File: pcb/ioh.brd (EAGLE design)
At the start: 100 x 80 mm, 23 parts, among them Q1 MOSFET-NCHANNEL2N7000, Q2 MOSFET-NCHANNEL2N7000, Q3 MOSFET-NCHANNEL2N7000, Q4 MOSFET-NCHANNEL2N7000

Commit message: some names
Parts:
- renumbered D1 to IRFRONT, D2 to IRBACK, JP3 to BZZ
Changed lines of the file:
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@@
 <element name="Q1" library="SparkFun-DiscreteSemi" package="TO-92" value="MOSFET-NCHANNEL2N7000" x="-52.07" y="71.12"/>
 <element name="R1" library="SparkFun-Resistors" package="AXIAL-0.4" value="20k" x="-62.23" y="69.85"/>
-<element name="D1" library="SparkFun-LED" package="LTE-302" value="" x="-66.04" y="-1.27"/>
+<element name="IRFRONT" library="SparkFun-LED" package="LTE-302" value="" x="-66.04" y="-1.27"/>
 <element name="R2" library="SparkFun-Resistors" package="AXIAL-0.4" value="20k" x="-62.23" y="-6.35"/>
 <element name="Q2" library="SparkFun-DiscreteSemi" package="TO-92" value="MOSFET-NCHANNEL2N7000" x="-64.77" y="-11.43"/>
-<element name="D2" library="SparkFun-LED" package="LTE-302" value="" x="-66.04" y="-24.13"/>
+<element name="IRBACK" library="SparkFun-LED" package="LTE-302" value="" x="-66.04" y="-24.13"/>
 <element name="R3" library="SparkFun-Resistors" package="AXIAL-0.4" value="20k" x="-62.23" y="-21.59"/>
 <element name="Q3" library="SparkFun-DiscreteSemi" package="TO-92" value="MOSFET-NCHANNEL2N7000" x="-64.77" y="-16.51"/>
@@
 <attribute name="PROD_ID" value="CAP-08440" x="-72.39" y="-30.48" size="1.778" layer="27" display="off"/>
 </element>
-<element name="JP3" library="SparkFun-Connectors" package="1X02" value="M02PTH" x="-72.39" y="-39.37"/>
+<element name="BZZ" library="SparkFun-Connectors" package="1X02" value="M02PTH" x="-72.39" y="-39.37"/>
 <element name="Q4" library="SparkFun-DiscreteSemi" package="TO-92" value="MOSFET-NCHANNEL2N7000" x="-71.12" y="-46.99"/>
 <element name="S1" library="adafruit" package="B3F-40XX" value="" x="-66.04" y="-58.42">
@@
 <contactref element="R2" pad="P$2"/>
 <contactref element="R3" pad="P$2"/>
-<contactref element="JP3" pad="1"/>
+<contactref element="BZZ" pad="1"/>
 <wire x1="-57.15" y1="-21.59" x2="-72.39" y2="-39.37" width="0" layer="19" extent="1-1"/>
 <wire x1="-57.15" y1="-6.35" x2="-57.15" y2="-21.59" width="0" layer="19" extent="1-1"/>
@@
 <signal name="N$4">
 <contactref element="R2" pad="P$1"/>
-<contactref element="D1" pad="A"/>
+<contactref element="IRFRONT" pad="A"/>
 <wire x1="-64.77" y1="-1.27" x2="-67.31" y2="-6.35" width="0" layer="19" extent="1-1"/>
 </signal>
 <signal name="N$11">
-<contactref element="D1" pad="C"/>
+<contactref element="IRFRONT" pad="C"/>
 <contactref element="Q2" pad="3"/>
 <wire x1="-67.31" y1="-1.27" x2="-63.5" y2="-11.43" width="0" layer="19" extent="1-1"/>
@@
 <signal name="N$24">
 <contactref element="R3" pad="P$1"/>
-<contactref element="D2" pad="A"/>
+<contactref element="IRBACK" pad="A"/>
 <wire x1="-64.77" y1="-24.13" x2="-67.31" y2="-21.59" width="0" layer="19" extent="1-1"/>
 </signal>
 <signal name="N$25">
-<contactref element="D2" pad="C"/>
+<contactref element="IRBACK" pad="C"/>
 <contactref element="Q3" pad="3"/>
 <wire x1="-63.5" y1="-16.51" x2="-67.31" y2="-24.13" width="0" layer="19" extent="1-1"/>
@@
 <signal name="N$13">
 <contactref element="Q4" pad="3"/>
-<contactref element="JP3" pad="2"/>
+<contactref element="BZZ" pad="2"/>
 <wire x1="-69.85" y1="-39.37" x2="-69.85" y2="-46.99" width="0" layer="19" extent="1-1"/>
 </signal>

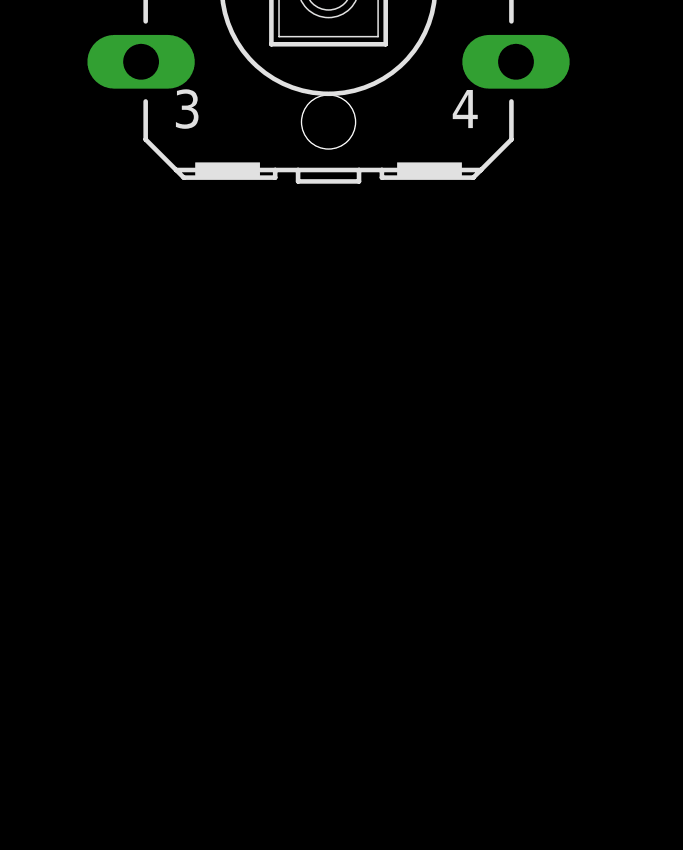
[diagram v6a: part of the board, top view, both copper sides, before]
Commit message: power test points
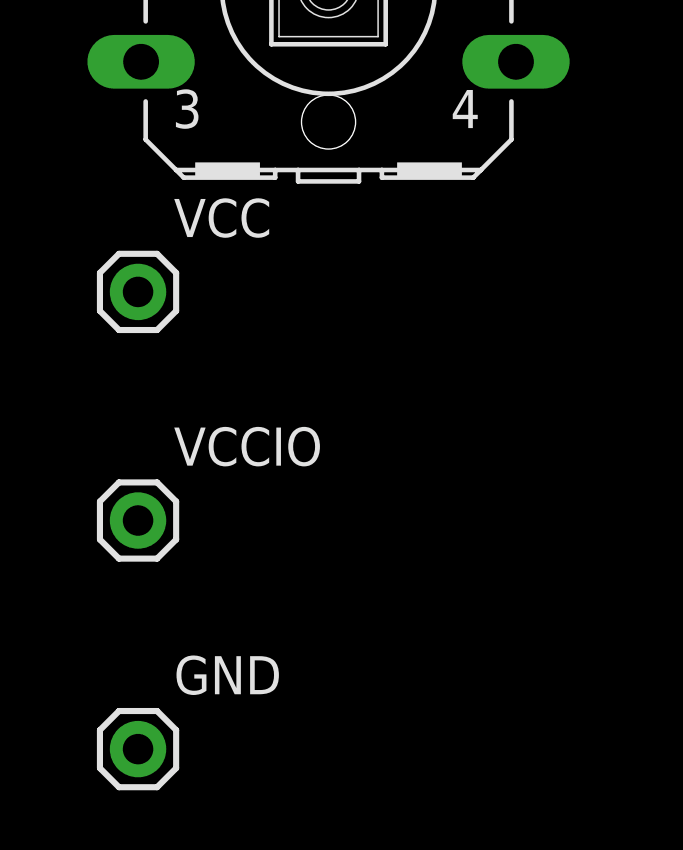
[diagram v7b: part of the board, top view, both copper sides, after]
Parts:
- added GND, VCC, VCCIO: M01PTH, SparkFun-Connectors:1X01
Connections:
- net GND: now also GND.1
- net VCC: now also VCC.1
- net VCCIO: now also VCCIO.1
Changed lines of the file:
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@@
 <attribute name="OC_FARNELL" value="176434" x="-66.04" y="-58.42" size="1.778" layer="27" display="off"/>
 </element>
+<element name="VCC" library="SparkFun-Connectors" package="1X01" value="M01PTH" x="-72.39" y="-68.58"/>
+<element name="VCCIO" library="SparkFun-Connectors" package="1X01" value="M01PTH" x="-72.39" y="-76.2"/>
+<element name="GND" library="SparkFun-Connectors" package="1X01" value="M01PTH" x="-72.39" y="-83.82"/>
 </elements>
 <signals>
@@
 <contactref element="S1" pad="3"/>
 <contactref element="S1" pad="4"/>
+<contactref element="GND" pad="1"/>
+<wire x1="-72.2884" y1="-60.9092" x2="-72.39" y2="-83.82" width="0" layer="19" extent="1-1"/>
 <wire x1="-59.7916" y1="-60.9092" x2="-72.2884" y2="-60.9092" width="0" layer="19" extent="1-1"/>
 <wire x1="-72.39" y1="-46.99" x2="-72.2884" y2="-60.9092" width="0" layer="19" extent="1-1"/>
@@
 <contactref element="RXBACK" pad="VS"/>
 <contactref element="C1" pad="1"/>
-<wire x1="-60.96" y1="-33.02" x2="-71.12" y2="-30.48" width="0" layer="19" extent="1-1"/>
+<contactref element="VCCIO" pad="1"/>
+<wire x1="-60.96" y1="-33.02" x2="-72.39" y2="-76.2" width="0" layer="19" extent="1-1"/>
 <wire x1="-60.96" y1="-27.94" x2="-60.96" y2="-33.02" width="0" layer="19" extent="1-1"/>
+<wire x1="-71.12" y1="-30.48" x2="-60.96" y2="-33.02" width="0" layer="19" extent="1-1"/>
 <wire x1="-40.22" y1="11.43" x2="-60.96" y2="-27.94" width="0" layer="19" extent="1-1"/>
 <wire x1="-36.4" y1="27.62" x2="-40.22" y2="11.43" width="0" layer="19" extent="1-1"/>
@@
 <contactref element="R3" pad="P$2"/>
 <contactref element="BZZ" pad="1"/>
+<contactref element="VCC" pad="1"/>
+<wire x1="-72.39" y1="-39.37" x2="-72.39" y2="-68.58" width="0" layer="19" extent="1-1"/>
 <wire x1="-57.15" y1="-21.59" x2="-72.39" y2="-39.37" width="0" layer="19" extent="1-1"/>
 <wire x1="-57.15" y1="-6.35" x2="-57.15" y2="-21.59" width="0" layer="19" extent="1-1"/>

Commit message: OSH
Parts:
- added LOGO1: OSHW-LOGOS, SparkFun-Aesthetics:OSHW-LOGO-S
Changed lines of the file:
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@@
 <element name="VCCIO" library="SparkFun-Connectors" package="1X01" value="M01PTH" x="-72.39" y="-76.2"/>
 <element name="GND" library="SparkFun-Connectors" package="1X01" value="M01PTH" x="-72.39" y="-83.82"/>
+<element name="LOGO1" library="SparkFun-Aesthetics" package="OSHW-LOGO-S" value="OSHW-LOGOS" x="-72.39" y="-90.17"/>
 </elements>
 <signals>
